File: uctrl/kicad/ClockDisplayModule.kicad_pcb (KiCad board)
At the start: 2 copper layers, 91.4 x 58.4 mm, 48 parts, among them IC1 ATMEGA88PA-A, P101 CONN_02X03, P102 CONN_01X06, P201 CONN_01X06, P202 CONN_01X07, P203 CONN_01X06, P204 CONN_01X07, Q201 BC856BS, Q202 BC856BS, Q203 BC856BS, SW101 SW_PUSH, U201 SN74LS138, U202 74HC4511

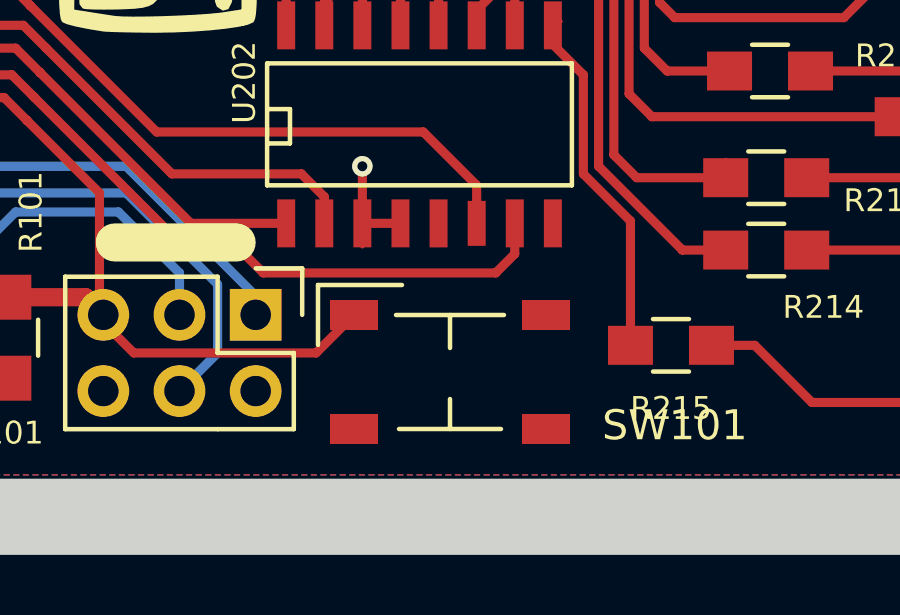
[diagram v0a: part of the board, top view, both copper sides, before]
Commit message: Updated the reset switch symbol and footprint
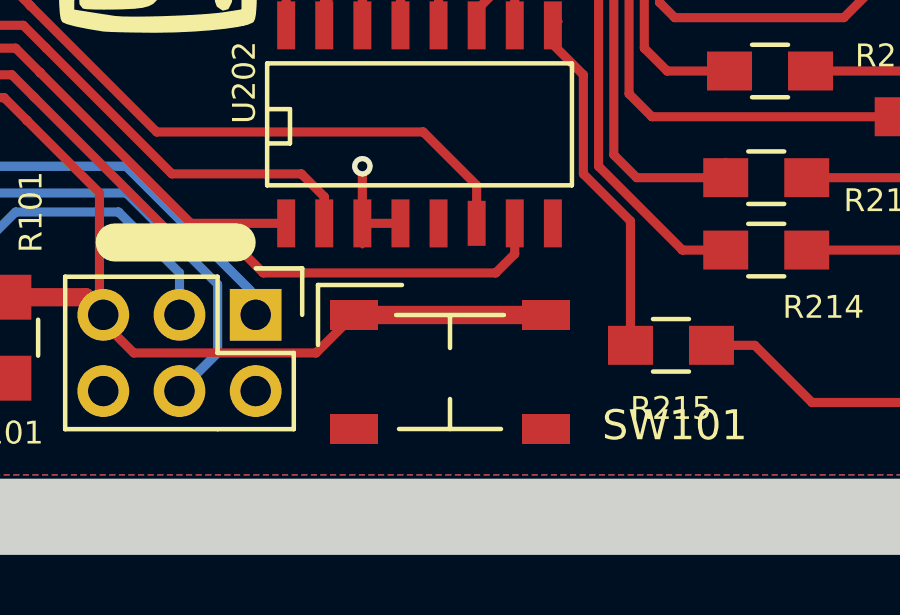
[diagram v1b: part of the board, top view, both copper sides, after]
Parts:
- SW101: value SW_PUSH -> TL3315NF160Q
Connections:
- SW101 pad 2: GND -> Reset
- SW101 pad 3: (no net) -> GND
- SW101 pad 4: (no net) -> GND
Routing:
- net Reset: track 30.0 -> 36.4 mm
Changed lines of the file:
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@@
-(kicad_pcb (version 4) (host pcbnew 0.201508140901+6091~28~ubuntu14.04.1-product)
+(kicad_pcb (version 4) (host pcbnew 4.0.1-2.201512121406+6195~38~ubuntu14.04.1-stable)
   (general
-    (links 128)
+    (links 130)
     (no_connects 0)
     (area 114.299999 40.639999 208.280001 101.600001)
     (thickness 1.6)
     (drawings 20)
-    (tracks 595)
+    (tracks 596)
     (zones 0)
     (modules 48)
@@
   )
   (setup
-    (last_trace_width 0.1524)
+    (last_trace_width 0.6096)
     (user_trace_width 0.3048)
     (user_trace_width 0.6096)
@@
       (effects (font (size 1 1) (thickness 0.15)))
     )
-    (fp_text value SW_PUSH (at 0 -4.7) (layer F.Fab) hide
+    (fp_text value TL3315NF160Q (at 0 -4.7) (layer F.Fab) hide
       (effects (font (size 1 1) (thickness 0.15)))
     )
@@
       (net 20 Reset))
     (pad 2 smd rect (at 3.2 -1.9) (size 1.6 1) (layers F.Cu F.Paste F.Mask)
+      (net 20 Reset))
+    (pad 3 smd rect (at -3.2 1.9) (size 1.6 1) (layers F.Cu F.Paste F.Mask)
       (net 13 GND))
-    (pad 3 smd rect (at -3.2 1.9) (size 1.6 1) (layers F.Cu F.Paste F.Mask))
-    (pad 4 smd rect (at 3.2 1.9) (size 1.6 1) (layers F.Cu F.Paste F.Mask))
+    (pad 4 smd rect (at 3.2 1.9) (size 1.6 1) (layers F.Cu F.Paste F.Mask)
+      (net 13 GND))
   )
   (gr_line (start 167.513 91.186) (end 171.577 91.186) (angle 90) (layer F.SilkS) (width 1.27))
@@
   (segment (start 195.58 47.21098) (end 195.80098 47.21098) (width 0.1524) (layer B.Cu) (net 18))
   (segment (start 195.58 59.77) (end 195.58 62.45098) (width 0.3048) (layer B.Cu) (net 19))
+  (segment (start 175.489 93.604) (end 181.889 93.604) (width 0.6096) (layer F.Cu) (net 20) (status C00000))
   (segment (start 167.132 93.599) (end 167.132 93.853) (width 0.3048) (layer F.Cu) (net 20))
   (segment (start 167.132 93.853) (end 168.148 94.869) (width 0.3048) (layer F.Cu) (net 20))

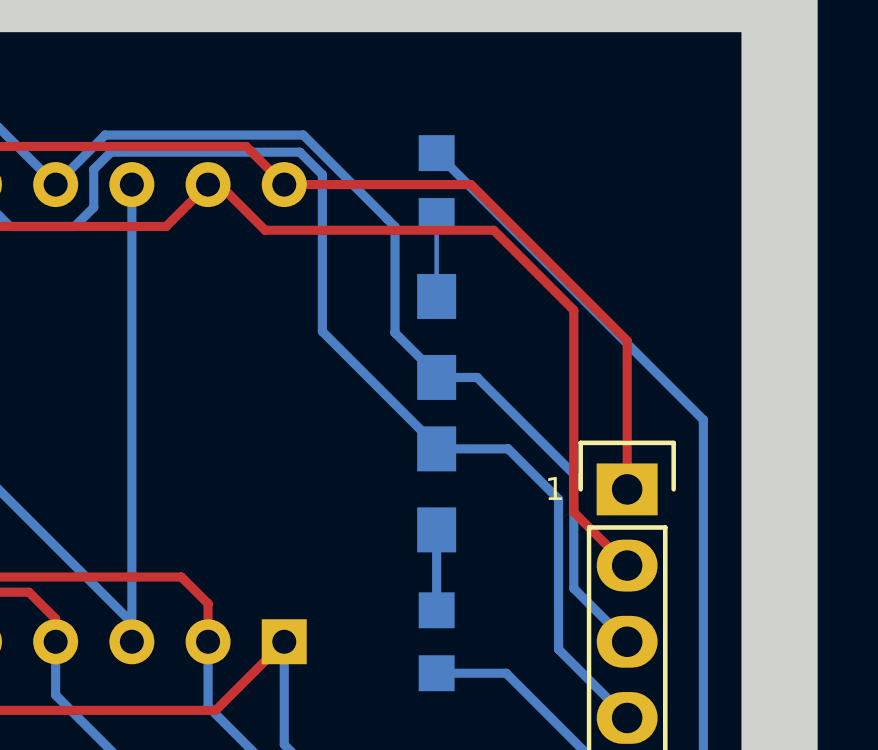
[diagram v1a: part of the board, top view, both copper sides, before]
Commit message: Correction to segments F and G!
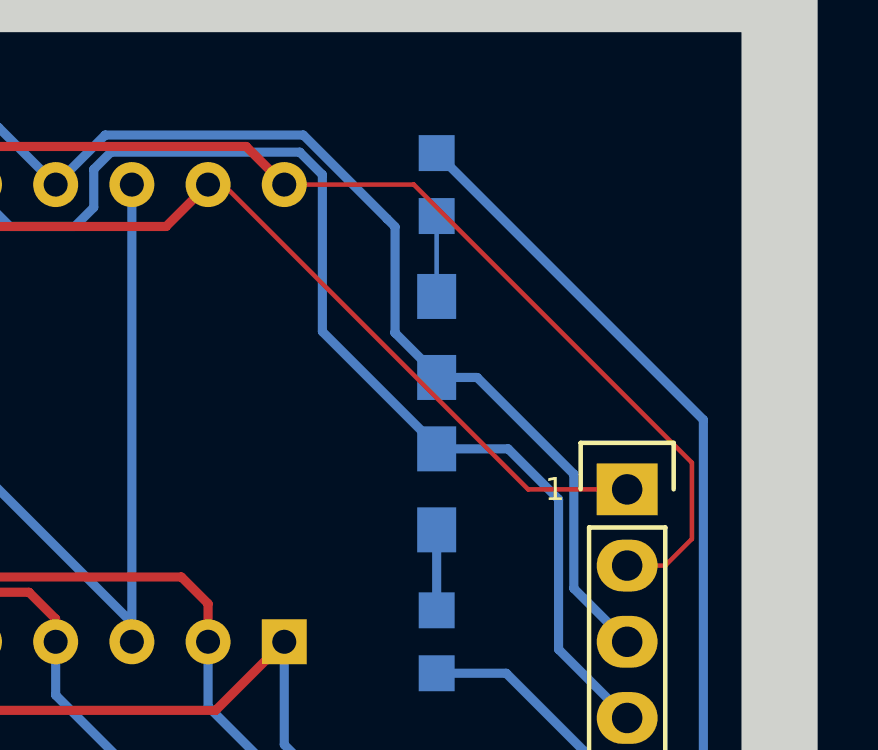
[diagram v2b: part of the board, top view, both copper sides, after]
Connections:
- P202 pad 1: /Display Driver/Seg_G -> /Display Driver/Seg_F
- P202 pad 2: /Display Driver/Seg_F -> /Display Driver/Seg_G
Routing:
- net /Display Driver/Seg_F: track 86.1 -> 81.4 mm
- net /Display Driver/Seg_G: track 79.3 -> 83.3 mm
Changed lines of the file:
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@@
-(kicad_pcb (version 4) (host pcbnew 4.0.1-2.201512121406+6195~38~ubuntu14.04.1-stable)
+(kicad_pcb (version 4) (host pcbnew 4.0.0-rc1-stable)
   (general
     (links 130)
@@
   )
   (setup
-    (last_trace_width 0.6096)
+    (last_trace_width 0.1524)
     (user_trace_width 0.3048)
     (user_trace_width 0.6096)
@@
     (pad_to_paste_clearance 0.0254)
     (aux_axis_origin 0 0)
-    (visible_elements FFFEFF7F)
+    (visible_elements 7FFEFFFF)
     (pcbplotparams
       (layerselection 0x010fc_80000001)
@@
     (fp_line (start -1.55 -1.55) (end 1.55 -1.55) (layer F.SilkS) (width 0.15))
     (pad 1 thru_hole rect (at 0 0) (size 2.032 1.7272) (drill 1.016) (layers *.Cu *.Mask F.SilkS)
+      (net 7 "/Display Driver/Seg_F"))
+    (pad 2 thru_hole oval (at 0 2.54) (size 2.032 1.7272) (drill 1.016) (layers *.Cu *.Mask F.SilkS)
       (net 8 "/Display Driver/Seg_G"))
-    (pad 2 thru_hole oval (at 0 2.54) (size 2.032 1.7272) (drill 1.016) (layers *.Cu *.Mask F.SilkS)
-      (net 7 "/Display Driver/Seg_F"))
     (pad 3 thru_hole oval (at 0 5.08) (size 2.032 1.7272) (drill 1.016) (layers *.Cu *.Mask F.SilkS)
       (net 6 "/Display Driver/Seg_A"))
@@
   (segment (start 129.54 48.26) (end 129.54 47.625) (width 0.1524) (layer F.Cu) (net 6))
   (segment (start 182.88 48.133) (end 182.88 48.26) (width 0.1524) (layer B.Cu) (net 6))
+  (segment (start 187.96 48.26) (end 188.468 48.26) (width 0.1524) (layer F.Cu) (net 7) (status C00000))
+  (segment (start 188.468 48.26) (end 198.628 58.42) (width 0.1524) (layer F.Cu) (net 7) (status 400000))
+  (segment (start 198.628 58.42) (end 201.93 58.42) (width 0.1524) (layer F.Cu) (net 7) (status 800000))
   (segment (start 187.96 48.26) (end 188.341 48.26) (width 0.3048) (layer F.Cu) (net 7))
-  (segment (start 188.341 48.26) (end 189.865 49.784) (width 0.3048) (layer F.Cu) (net 7))
-  (segment (start 200.152 59.182) (end 201.93 60.96) (width 0.3048) (layer F.Cu) (net 7))
-  (segment (start 200.152 52.451) (end 200.152 59.182) (width 0.3048) (layer F.Cu) (net 7))
-  (segment (start 197.485 49.784) (end 200.152 52.451) (width 0.3048) (layer F.Cu) (net 7))
-  (segment (start 189.865 49.784) (end 197.485 49.784) (width 0.3048) (layer F.Cu) (net 7))
   (segment (start 165.989 51.943) (end 153.289 51.943) (width 0.3048) (layer F.Cu) (net 7))
   (segment (start 172.72 48.26) (end 171.323 46.863) (width 0.3048) (layer F.Cu) (net 7))
@@
   (segment (start 134.62 48.26) (end 134.62 48.641) (width 0.1524) (layer B.Cu) (net 7))
   (segment (start 187.96 48.26) (end 187.96 48.768) (width 0.1524) (layer F.Cu) (net 7))
-  (segment (start 190.5 48.26) (end 196.723 48.26) (width 0.3048) (layer F.Cu) (net 8))
-  (segment (start 201.93 53.467) (end 201.93 58.42) (width 0.3048) (layer F.Cu) (net 8))
-  (segment (start 196.723 48.26) (end 201.93 53.467) (width 0.3048) (layer F.Cu) (net 8))
+  (segment (start 190.5 48.26) (end 194.818 48.26) (width 0.1524) (layer F.Cu) (net 8) (status 400000))
+  (segment (start 203.2 60.96) (end 201.93 60.96) (width 0.1524) (layer F.Cu) (net 8) (status 800000))
+  (segment (start 204.089 60.071) (end 203.2 60.96) (width 0.1524) (layer F.Cu) (net 8))
+  (segment (start 204.089 57.531) (end 204.089 60.071) (width 0.1524) (layer F.Cu) (net 8))
+  (segment (start 194.818 48.26) (end 204.089 57.531) (width 0.1524) (layer F.Cu) (net 8))
   (segment (start 137.16 48.26) (end 137.16 47.879) (width 0.1524) (layer F.Cu) (net 8))
   (segment (start 137.16 47.879) (end 138.684 46.355) (width 0.3048) (layer F.Cu) (net 8))
@@
   (segment (start 195.58 47.21098) (end 195.80098 47.21098) (width 0.1524) (layer B.Cu) (net 18))
   (segment (start 195.58 59.77) (end 195.58 62.45098) (width 0.3048) (layer B.Cu) (net 19))
-  (segment (start 175.489 93.604) (end 181.889 93.604) (width 0.6096) (layer F.Cu) (net 20) (status C00000))
+  (segment (start 175.489 93.604) (end 181.889 93.604) (width 0.6096) (layer F.Cu) (net 20))
   (segment (start 167.132 93.599) (end 167.132 93.853) (width 0.3048) (layer F.Cu) (net 20))
   (segment (start 167.132 93.853) (end 168.148 94.869) (width 0.3048) (layer F.Cu) (net 20))

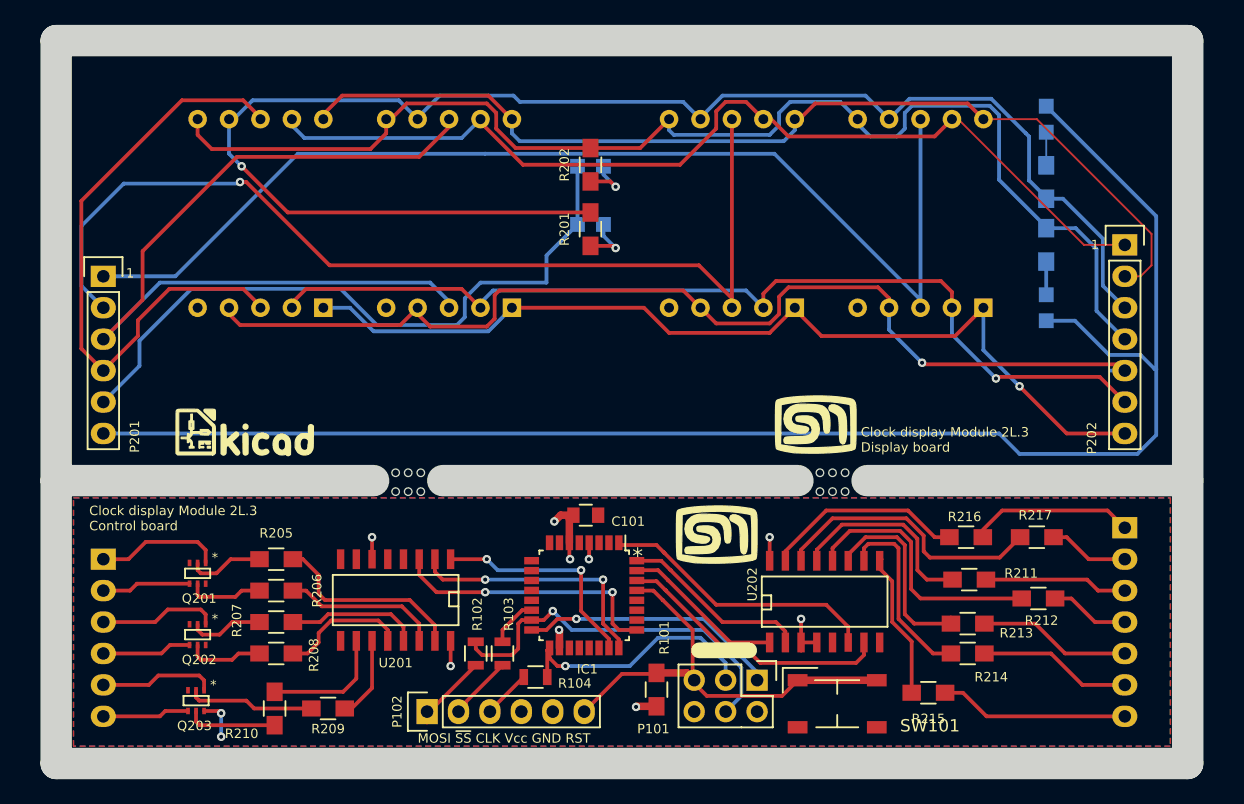
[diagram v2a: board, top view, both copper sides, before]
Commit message: Updated the seven segment foot print and added the mounting tabs
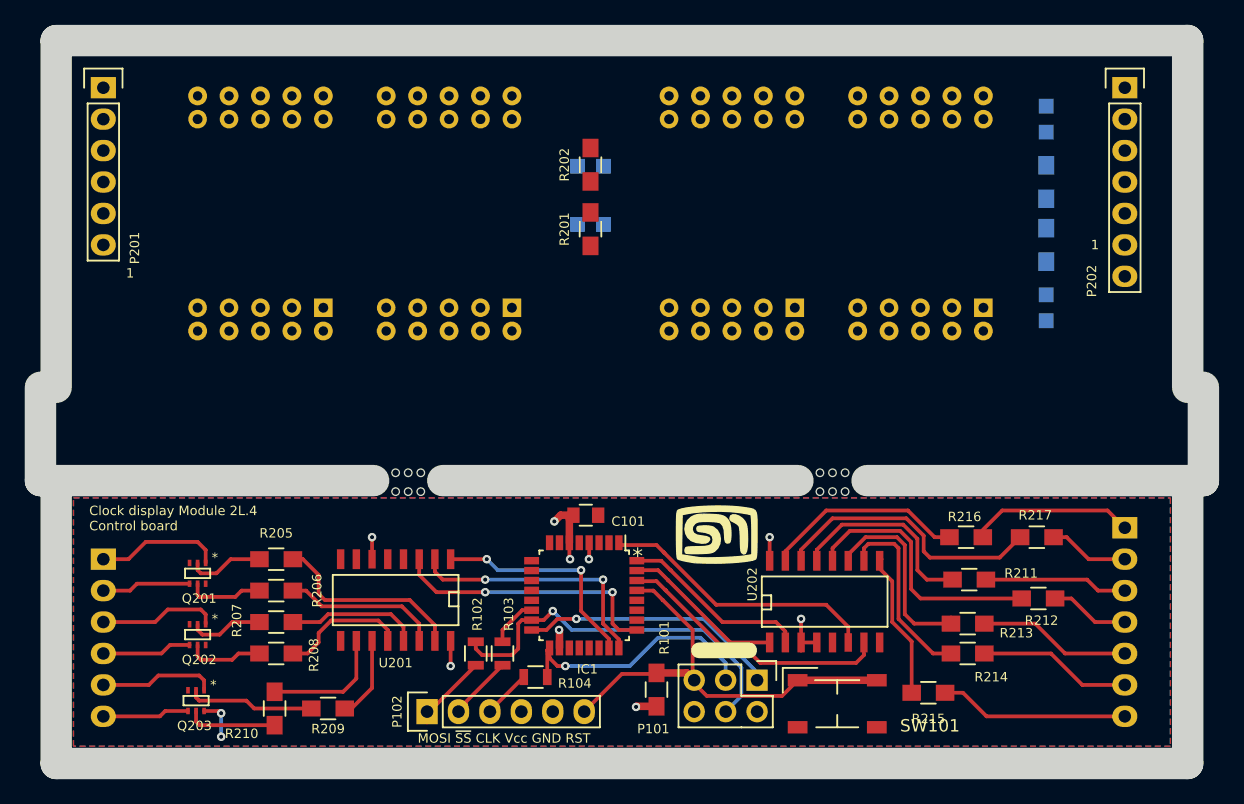
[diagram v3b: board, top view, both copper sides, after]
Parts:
- AFF201, AFF202, AFF203, AFF204: footprint ClockFootprints:161_163_Series -> ClockFootprints:161_163_Series_extended
- G*** (x2): moved to B.Cu
- moved G*** 67.6 mm to (198.4, 72.9), turned to 180 degrees
- moved G*** 36.2 mm to (140.7, 72.1), turned to 180 degrees
- moved P201 15.2 mm to (119.4, 45.7)
- moved P202 12.7 mm to (201.9, 45.7)
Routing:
- net D_Signal: track 127.4 -> 0.00 mm
- net /Display Driver/Seg_A: track 124.5 -> 0.00 mm, vias 1 -> 0
- net /Display Driver/Seg_B: track 102.7 -> 0.00 mm
- net D_Dig_0: track 90.9 -> 0.00 mm
- net /Display Driver/Seg_C: track 86.2 -> 0.00 mm, vias 1 -> 0
- net /Display Driver/Seg_G: track 83.3 -> 0.00 mm
- net /Display Driver/Seg_F: track 81.4 -> 0.00 mm
- net D_Dig_1: track 81.3 -> 0.00 mm, vias 1 -> 0
- net /Display Driver/Seg_D: track 78.7 -> 0.00 mm, vias 1 -> 0
- net /Display Driver/Seg_E: track 77.5 -> 0.00 mm, vias 1 -> 0
- net D_Dig_2: track 69.0 -> 0.00 mm
- net D_Colon: track 55.1 -> 0.00 mm
- net D_Dig_3: track 50.4 -> 0.00 mm
- net Net-(D201-Pad2): track 4.42 -> 0.00 mm, vias 1 -> 0
- net Net-(D202-Pad2): track 4.27 -> 0.00 mm, vias 1 -> 0
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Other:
- board size 91.4 x 58.4 mm -> 94 x 58.4 mm
- board text added: "Clock display Module 2L.4 Control board"
- board text added: "Clock display Module 2L.4 Display board"
- board text removed: "Clock display Module 2L.3 Control board"
- board text removed: "Clock display Module 2L.3 Display board"

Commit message: Started routing the modified board
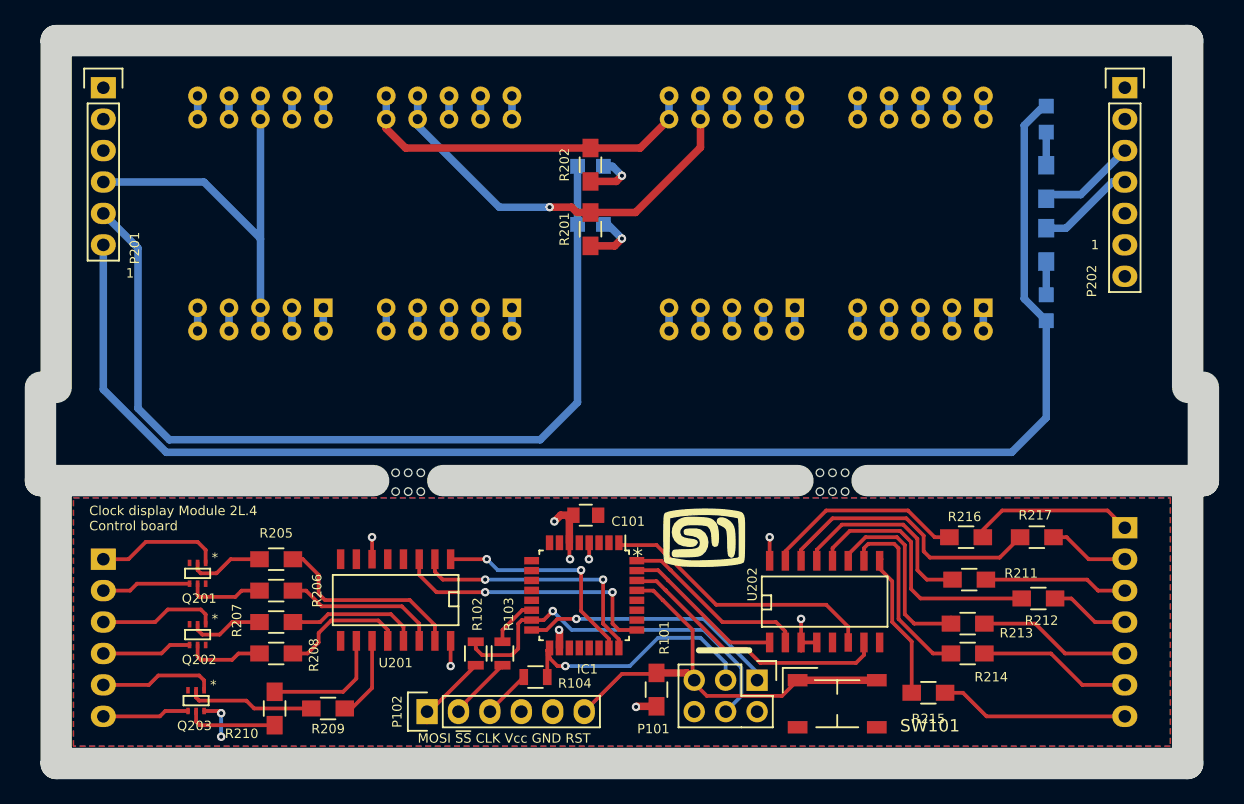
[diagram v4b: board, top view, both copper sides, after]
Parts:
- moved G*** 1.05 mm to (167.9, 82.0)
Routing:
- net D_Signal: track 0.00 -> 117.9 mm
- net D_Colon: track 0.00 -> 73.8 mm
- net /Display Driver/Seg_A: track 0.00 -> 46.2 mm, vias 0 -> 1
- net /Display Driver/Seg_B: track 0.00 -> 40.7 mm
- net D_Dig_3: track 0.00 -> 33.6 mm
- net /Display Driver/Seg_G: track 0.00 -> 7.52 mm
- net /Display Driver/Seg_F: track 0.00 -> 7.52 mm
- net /Display Driver/Seg_E: track 0.00 -> 7.52 mm
- net /Display Driver/Seg_D: track 0.00 -> 7.52 mm
- net /Display Driver/Seg_C: track 0.00 -> 7.52 mm
- net Net-(D201-Pad2): track 0.00 -> 4.84 mm, vias 0 -> 1
- net Net-(D202-Pad2): track 0.00 -> 4.54 mm, vias 0 -> 1
- net D_Dig_2: track 0.00 -> 3.76 mm
- net D_Dig_1: track 0.00 -> 3.76 mm
- net D_Dig_0: track 0.00 -> 3.76 mm
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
